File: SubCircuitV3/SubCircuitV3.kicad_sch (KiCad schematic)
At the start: 32 parts, among them J1 JTAG, J10 ESC_POWER, J11 ESC_POWER, J12 ESC_POWER, J13 ESC_POWER, J14 FEMALE XT-60, J15 ESC PWM, J16 3S, J17 Water Sensor Input, J2 ESC PWM, J3 ESC PWM, J4 ESC PWM, J5 ESC PWM, J6 ESC PWM, J7 5S, J8 ESC_POWER, J9 ESC_POWER, K1 G5Q-1A, Q1 NMOS, Q2 NMOS, Q3 NMOS, Q4 NMOS, Q5 NMOS, Q6 NMOS

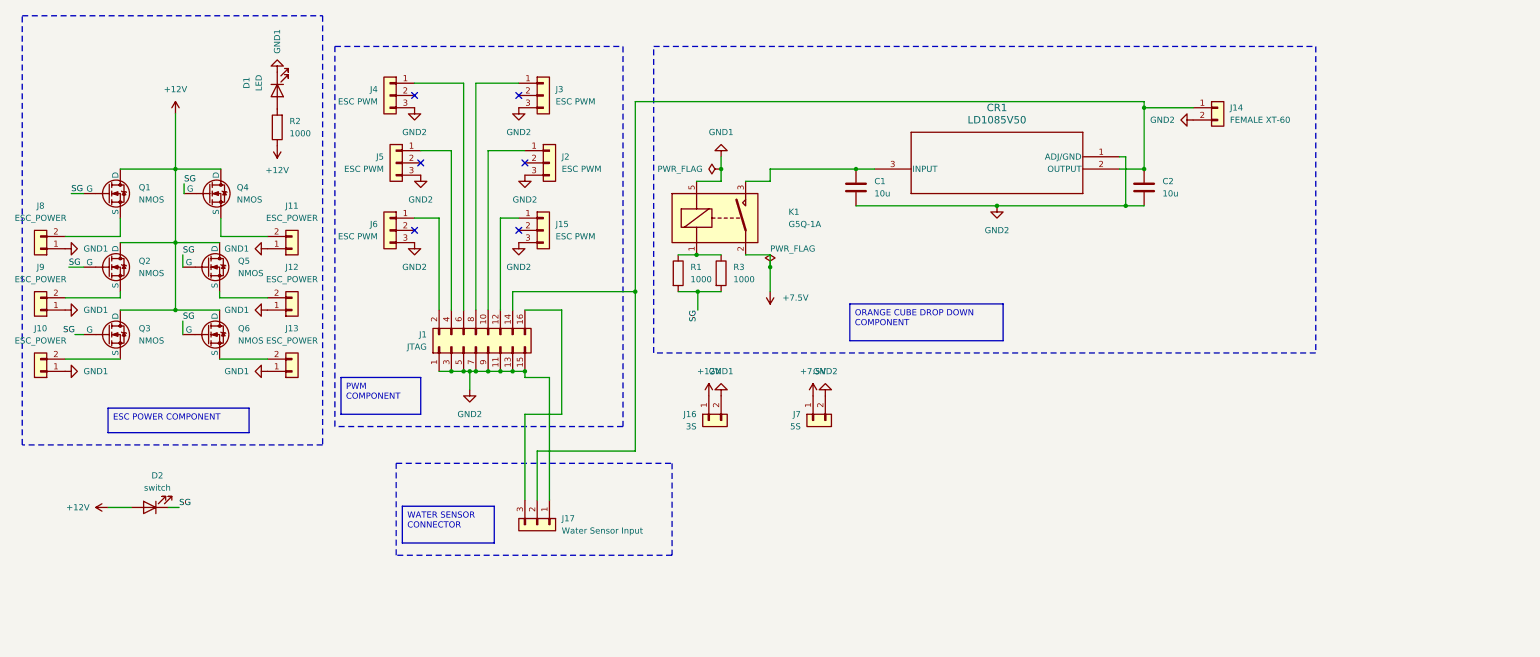
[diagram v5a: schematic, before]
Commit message: Added fuses, mosfets, and updated power ports
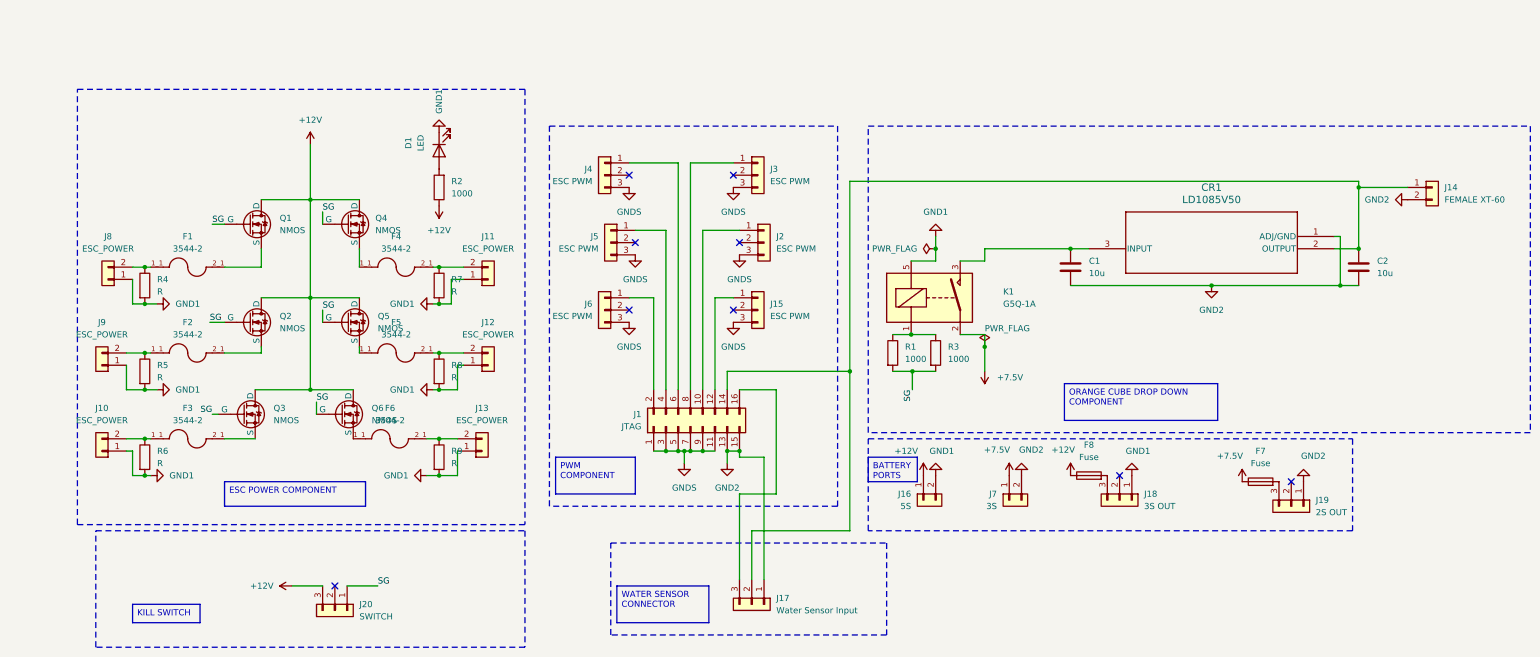
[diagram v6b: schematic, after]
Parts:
- removed D2: switch, LED_THT:LED_D5.0mm_Horizontal_O6.35mm_Z9.0mm, symbol Device:LED
- added F1, F2, F3, F4, F5, F6: 3544-2, 3544-2:FUSE_3544-2, symbol RoboSub_Lib:3544-2
- added F7, F8: Fuse, Resistor_THT:R_Axial_DIN0411_L9.9mm_D3.6mm_P20.32mm_Horizontal, symbol Device:Fuse
- added J18: 3S OUT, 284932-3:CONN3_284392-3_TEC, symbol Connector_Generic:Conn_01x03
- added J19: 2S OUT, 284932-3:CONN3_284392-3_TEC, symbol Connector_Generic:Conn_01x03
- added J20: SWITCH, 284932-3:CONN3_284392-3_TEC, symbol Connector_Generic:Conn_01x03
- added R4, R5, R6, R7, R8, R9: R, Resistor_THT:R_Axial_DIN0207_L6.3mm_D2.5mm_P10.16mm_Horizontal, symbol Device:R
- J16: value 3S -> 5S; footprint AMASS_XT60-M:AMASS_XT60-M_1x02_P7.20mm_Vertical -> Connector_AMASS:AMASS_XT90PW-M_1x02_P10.90mm_Horizontal
- J7: value 5S -> 3S; footprint AMASS_XT60-M:AMASS_XT60-M_1x02_P7.20mm_Vertical -> Connector_AMASS:AMASS_XT90PW-M_1x02_P10.90mm_Horizontal
- Q1, Q2, Q3, Q4, Q5, Q6: footprint BSZ065N03LSATMA1-MOSFET:BSZ065N03LSATMA1 -> AOD454:AOD454A
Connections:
- net +12V: now also F8.1, J20.3 (Pin_3)
- net +7.5V: now also F7.1
- net GND1: now also J18.1 (Pin_1), R4.2, R5.2, R6.2, R7.2, R8.2, R9.2
- net GND2: now also J19.1 (Pin_1); no longer J1.1 (Pin_1), J1.11 (Pin_11), J1.3 (Pin_3), J1.5 (Pin_5), J1.7 (Pin_7), J1.9 (Pin_9), J15.3 (Pin_3), J2.3 (Pin_3), J3.3 (Pin_3), J4.3 (Pin_3), J5.3 (Pin_3), J6.3 (Pin_3)
- net SG: now also J20.1 (Pin_1)
- net at Q5.3 (S): now also F5.1_1; no longer J12.2 (Pin_2)
- net at Q3.3 (S): now also F3.2_1; no longer J10.2 (Pin_2)
- net at J11.2 (Pin_2): now also F4.2_1, R7.1; no longer Q4.3 (S)
- net at J9.2 (Pin_2): now also F2.1_1, R5.1; no longer Q2.3 (S)
- net at J8.2 (Pin_2): now also F1.1_1, R4.1; no longer Q1.3 (S)
- net at Q6.3 (S): now also F6.1_1; no longer J13.2 (Pin_2)
- new net: F7.2, J19.3 (Pin_3)
- new net: F5.2_1, J12.2 (Pin_2), R8.1
- new net: F4.1_1, Q4.3 (S)
- new net: F2.2_1, Q2.3 (S)
- new net: F6.2_1, J13.2 (Pin_2), R9.1
- new net: F8.2, J18.3 (Pin_3)
- new net: F3.1_1, J10.2 (Pin_2), R6.1
- new net: F1.2_1, Q1.3 (S)
- new net GNDS: J1.1 (Pin_1), J1.11 (Pin_11), J1.3 (Pin_3), J1.5 (Pin_5), J1.7 (Pin_7), J1.9 (Pin_9), J15.3 (Pin_3), J2.3 (Pin_3), J3.3 (Pin_3), J4.3 (Pin_3), J5.3 (Pin_3), J6.3 (Pin_3)
- no-connect marks 6 -> 9
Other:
- moved on the sheet: C1, C2, CR1, D1, J1, J10, J11, J12, J13, J14, J15, J16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

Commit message: Update pin header and xt90 footprintg
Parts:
- J1: footprint Connector_PinHeader_2.00mm:PinHeader_2x08_P2.00mm_Vertical -> Connector_PinHeader_2.54mm:PinHeader_2x08_P2.54mm_Vertical
- J16, J7: footprint Connector_AMASS:AMASS_XT90PW-M_1x02_P10.90mm_Horizontal -> Footprints:XT90
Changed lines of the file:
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@@
 			)
 		)
-		(property "Footprint" "Connector_AMASS:AMASS_XT90PW-M_1x02_P10.90mm_Horizontal"
+		(property "Footprint" "Footprints:XT90"
 			(at 219.71 163.83 0)
 			(effects
@@
 			)
 		)
-		(property "Footprint" "Connector_PinHeader_2.00mm:PinHeader_2x08_P2.00mm_Vertical"
+		(property "Footprint" "Connector_PinHeader_2.54mm:PinHeader_2x08_P2.54mm_Vertical"
 			(at 153.67 148.59 0)
 			(effects
@@
 			)
 		)
-		(property "Footprint" "Connector_AMASS:AMASS_XT90PW-M_1x02_P10.90mm_Horizontal"
+		(property "Footprint" "Footprints:XT90"
 			(at 201.93 163.83 0)
 			(effects

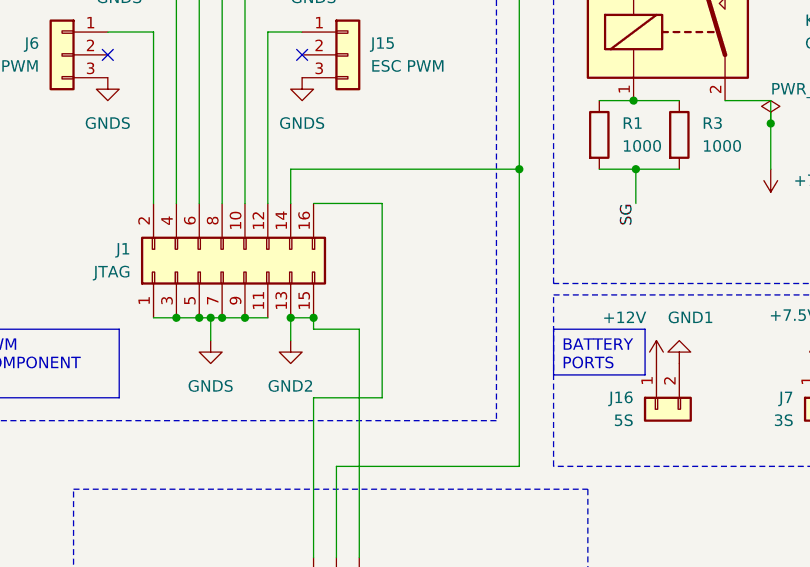
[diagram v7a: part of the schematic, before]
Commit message: Larger routing wires
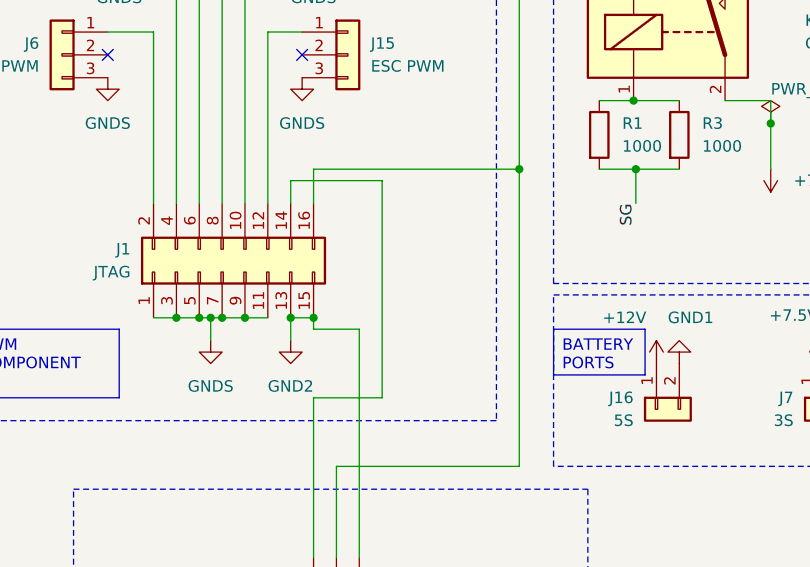
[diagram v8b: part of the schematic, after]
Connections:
- net at C2.1, CR1.2 (OUTPUT), J14.1 (Pin_1)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: now also J1.16 (Pin_16); no longer J1.14 (Pin_14)
- net at J17.3 (Pin_3): now also J1.14 (Pin_14); no longer J1.16 (Pin_16)
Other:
- title: Sub PDB V3 -> Sub PDB V4
